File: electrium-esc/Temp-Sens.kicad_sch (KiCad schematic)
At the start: 0 parts

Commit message: Add additional connections to MCU
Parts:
- added TH? (x2): Thermistor_PTC, symbol Device:Thermistor_PTC
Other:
- company: (none) -> Electrium Mobility
- title: (none) -> BLDC Electronic Speed Controller 1.0
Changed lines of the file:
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@@
 (kicad_sch (version 20211123) (generator eeschema)
   (paper "A4")
+  (title_block
+    (title "BLDC Electronic Speed Controller 1.0")
+    (rev "ESC 1.0")
+    (company "Electrium Mobility")
+    (comment 1 "Temp Sensors")
+  )
+  (symbol (lib_id "Device:Thermistor_PTC") (at 181.61 95.25 0) (unit 1)
+    (in_bom yes) (on_board yes) (fields_autoplaced)
+    (property "Reference" "TH?" (id 0) (at 184.15 94.2974 0)
+      (effects (font (size 1.27 1.27)) (justify left))
+    )
+    (property "Value" "Thermistor_PTC" (id 1) (at 184.15 96.8374 0)
+      (effects (font (size 1.27 1.27)) (justify left))
+    )
+    (property "Footprint" "" (id 2) (at 182.88 100.33 0)
+      (effects (font (size 1.27 1.27)) (justify left) hide)
+    )
+    (property "Datasheet" "~" (id 3) (at 181.61 95.25 0)
+      (effects (font (size 1.27 1.27)) hide)
+    )
+    (pin "1")
+    (pin "2")
+  )
+  (symbol (lib_id "Device:Thermistor_PTC") (at 153.67 95.25 0) (unit 1)
+    (in_bom yes) (on_board yes) (fields_autoplaced)
+    (property "Reference" "TH?" (id 0) (at 156.21 94.2974 0)
+      (effects (font (size 1.27 1.27)) (justify left))
+    )
+    (property "Value" "Thermistor_PTC" (id 1) (at 156.21 96.8374 0)
+      (effects (font (size 1.27 1.27)) (justify left))
+    )
+    (property "Footprint" "" (id 2) (at 154.94 100.33 0)
+      (effects (font (size 1.27 1.27)) (justify left) hide)
+    )
+    (property "Datasheet" "~" (id 3) (at 153.67 95.25 0)
+      (effects (font (size 1.27 1.27)) hide)
+    )
+    (pin "1")
+    (pin "2")
+  )
 )

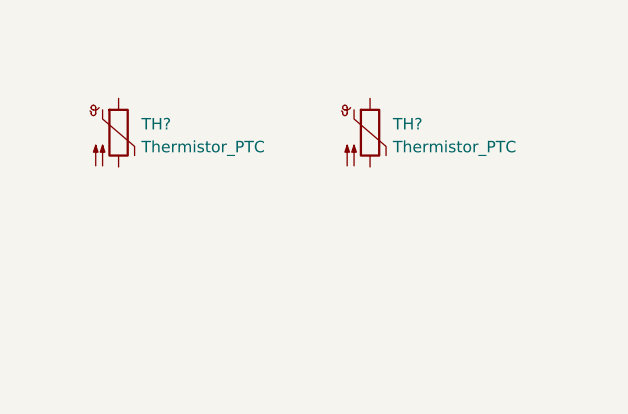
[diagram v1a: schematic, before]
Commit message: Connect Temperature Sensors
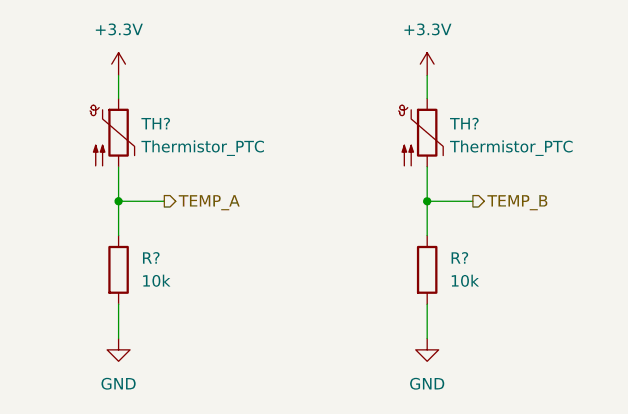
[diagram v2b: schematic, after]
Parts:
- added R? (x2): 10k, symbol Device:R
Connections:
- net +3.3V: now reaches TH?.1
- net +3.3V: now also TH?.1
- net TEMP_B: now reaches TH?.2
- net TEMP_B: now also R?.1
- net TEMP_A: now reaches TH?.2
- net TEMP_A: now also R?.1
- new net GND: R?.2, R?.2
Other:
- moved on the sheet: TH?
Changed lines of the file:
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@@
     (comment 1 "Temp Sensors")
   )
-  (symbol (lib_id "Device:Thermistor_PTC") (at 181.61 95.25 0) (unit 1)
+  (junction (at 187.96 102.87) (diameter 0) (color 0 0 0 0)
+  )
+  (junction (at 153.67 102.87) (diameter 0) (color 0 0 0 0)
+  )
+  (wire (pts (xy 153.67 102.87) (xy 158.75 102.87))
+    (stroke (width 0) (type default) (color 0 0 0 0))
+  )
+  (wire (pts (xy 153.67 88.9) (xy 153.67 91.44))
+    (stroke (width 0) (type default) (color 0 0 0 0))
+  )
+  (wire (pts (xy 153.67 114.3) (xy 153.67 118.11))
+    (stroke (width 0) (type default) (color 0 0 0 0))
+  )
+  (wire (pts (xy 153.67 102.87) (xy 153.67 106.68))
+    (stroke (width 0) (type default) (color 0 0 0 0))
+  )
+  (wire (pts (xy 187.96 102.87) (xy 187.96 106.68))
+    (stroke (width 0) (type default) (color 0 0 0 0))
+  )
+  (wire (pts (xy 187.96 114.3) (xy 187.96 118.11))
+    (stroke (width 0) (type default) (color 0 0 0 0))
+  )
+  (wire (pts (xy 187.96 88.9) (xy 187.96 91.44))
+    (stroke (width 0) (type default) (color 0 0 0 0))
+  )
+  (wire (pts (xy 187.96 99.06) (xy 187.96 102.87))
+    (stroke (width 0) (type default) (color 0 0 0 0))
+  )
+  (wire (pts (xy 187.96 102.87) (xy 193.04 102.87))
+    (stroke (width 0) (type default) (color 0 0 0 0))
+  )
+  (wire (pts (xy 153.67 99.06) (xy 153.67 102.87))
+    (stroke (width 0) (type default) (color 0 0 0 0))
+  )
+  (hierarchical_label "TEMP_B" (shape output) (at 193.04 102.87 0)
+    (effects (font (size 1.27 1.27)) (justify left))
+  )
+  (hierarchical_label "TEMP_A" (shape output) (at 158.75 102.87 0)
+    (effects (font (size 1.27 1.27)) (justify left))
+  )
+  (symbol (lib_id "power:GND") (at 153.67 118.11 0) (unit 1)
     (in_bom yes) (on_board yes) (fields_autoplaced)
-    (property "Reference" "TH?" (id 0) (at 184.15 94.2974 0)
+    (property "Reference" "#PWR?" (id 0) (at 153.67 124.46 0)
+      (effects (font (size 1.27 1.27)) hide)
+    )
+    (property "Value" "GND" (id 1) (at 153.67 123.19 0))
+    (property "Footprint" "" (id 2) (at 153.67 118.11 0)
+      (effects (font (size 1.27 1.27)) hide)
+    )
+    (property "Datasheet" "" (id 3) (at 153.67 118.11 0)
+      (effects (font (size 1.27 1.27)) hide)
+    )
+    (pin "1")
+  )
+  (symbol (lib_id "Device:Thermistor_PTC") (at 187.96 95.25 0) (unit 1)
+    (in_bom yes) (on_board yes) (fields_autoplaced)
+    (property "Reference" "TH?" (id 0) (at 190.5 94.2974 0)
       (effects (font (size 1.27 1.27)) (justify left))
     )
-    (property "Value" "Thermistor_PTC" (id 1) (at 184.15 96.8374 0)
+    (property "Value" "Thermistor_PTC" (id 1) (at 190.5 96.8374 0)
       (effects (font (size 1.27 1.27)) (justify left))
     )
-    (property "Footprint" "" (id 2) (at 182.88 100.33 0)
+    (property "Footprint" "" (id 2) (at 189.23 100.33 0)
       (effects (font (size 1.27 1.27)) (justify left) hide)
     )
-    (property "Datasheet" "~" (id 3) (at 181.61 95.25 0)
+    (property "Datasheet" "~" (id 3) (at 187.96 95.25 0)
       (effects (font (size 1.27 1.27)) hide)
     )
     (pin "1")
     (pin "2")
+  )
+  (symbol (lib_id "Device:R") (at 153.67 110.49 0) (unit 1)
+    (in_bom yes) (on_board yes) (fields_autoplaced)
+    (property "Reference" "R?" (id 0) (at 156.21 109.2199 0)
+      (effects (font (size 1.27 1.27)) (justify left))
+    )
+    (property "Value" "10k" (id 1) (at 156.21 111.7599 0)
+      (effects (font (size 1.27 1.27)) (justify left))
+    )
+    (property "Footprint" "" (id 2) (at 151.892 110.49 90)
+      (effects (font (size 1.27 1.27)) hide)
+    )
+    (property "Datasheet" "~" (id 3) (at 153.67 110.49 0)
+      (effects (font (size 1.27 1.27)) hide)
+    )
+    (pin "1")
+    (pin "2")
+  )
+  (symbol (lib_id "power:GND") (at 187.96 118.11 0) (unit 1)
+    (in_bom yes) (on_board yes) (fields_autoplaced)
+    (property "Reference" "#PWR?" (id 0) (at 187.96 124.46 0)
+      (effects (font (size 1.27 1.27)) hide)
+    )
+    (property "Value" "GND" (id 1) (at 187.96 123.19 0))
+    (property "Footprint" "" (id 2) (at 187.96 118.11 0)
+      (effects (font (size 1.27 1.27)) hide)
+    )
+    (property "Datasheet" "" (id 3) (at 187.96 118.11 0)
+      (effects (font (size 1.27 1.27)) hide)
+    )
+    (pin "1")
+  )
+  (symbol (lib_id "power:+3.3V") (at 153.67 88.9 0) (unit 1)
+    (in_bom yes) (on_board yes) (fields_autoplaced)
+    (property "Reference" "#PWR?" (id 0) (at 153.67 92.71 0)
+      (effects (font (size 1.27 1.27)) hide)
+    )
+    (property "Value" "+3.3V" (id 1) (at 153.67 83.82 0))
+    (property "Footprint" "" (id 2) (at 153.67 88.9 0)
+      (effects (font (size 1.27 1.27)) hide)
+    )
+    (property "Datasheet" "" (id 3) (at 153.67 88.9 0)
+      (effects (font (size 1.27 1.27)) hide)
+    )
+    (pin "1")
+  )
+  (symbol (lib_id "power:+3.3V") (at 187.96 88.9 0) (unit 1)
+    (in_bom yes) (on_board yes) (fields_autoplaced)
+    (property "Reference" "#PWR?" (id 0) (at 187.96 92.71 0)
+      (effects (font (size 1.27 1.27)) hide)
+    )
+    (property "Value" "+3.3V" (id 1) (at 187.96 83.82 0))
+    (property "Footprint" "" (id 2) (at 187.96 88.9 0)
+      (effects (font (size 1.27 1.27)) hide)
+    )
+    (property "Datasheet" "" (id 3) (at 187.96 88.9 0)
+      (effects (font (size 1.27 1.27)) hide)
+    )
+    (pin "1")
   )
   (symbol (lib_id "Device:Thermistor_PTC") (at 153.67 95.25 0) (unit 1)
@@
       (effects (font (size 1.27 1.27)) hide)
     )
+    (pin "1")
+    (pin "2")
+  )
+  (symbol (lib_id "Device:R") (at 187.96 110.49 0) (unit 1)
+    (in_bom yes) (on_board yes) (fields_autoplaced)
+    (property "Reference" "R?" (id 0) (at 190.5 109.2199 0)
+      (effects (font (size 1.27 1.27)) (justify left))
+    )
+    (property "Value" "10k" (id 1) (at 190.5 111.7599 0)
+      (effects (font (size 1.27 1.27)) (justify left))
+    )
+    (property "Footprint" "" (id 2) (at 186.182 110.49 90)
+      (effects (font (size 1.27 1.27)) hide)
+    )
+    (property "Datasheet" "~" (id 3) (at 187.96 110.49 0)
+      (effects (font (size 1.27 1.27)) hide)
+    )

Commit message: Modify title
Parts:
- added C? (x2): 2.2u, symbol Device:C
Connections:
- net GND: now also C?.2, C?.2
- net TEMP_A: now also C?.1
- net TEMP_B: now also C?.1
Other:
- moved on the sheet: R?
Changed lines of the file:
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@@
     (comment 1 "Temp Sensors")
   )
+  (junction (at 153.67 116.84) (diameter 0) (color 0 0 0 0)
+  )
   (junction (at 187.96 102.87) (diameter 0) (color 0 0 0 0)
   )
   (junction (at 153.67 102.87) (diameter 0) (color 0 0 0 0)
   )
+  (junction (at 187.96 116.84) (diameter 0) (color 0 0 0 0)
+  )
+  (wire (pts (xy 187.96 116.84) (xy 187.96 118.11))
+    (stroke (width 0) (type default) (color 0 0 0 0))
+  )
   (wire (pts (xy 153.67 102.87) (xy 158.75 102.87))
     (stroke (width 0) (type default) (color 0 0 0 0))
@@
     (stroke (width 0) (type default) (color 0 0 0 0))
   )
-  (wire (pts (xy 153.67 114.3) (xy 153.67 118.11))
-    (stroke (width 0) (type default) (color 0 0 0 0))
-  )
-  (wire (pts (xy 153.67 102.87) (xy 153.67 106.68))
-    (stroke (width 0) (type default) (color 0 0 0 0))
-  )
-  (wire (pts (xy 187.96 102.87) (xy 187.96 106.68))
-    (stroke (width 0) (type default) (color 0 0 0 0))
-  )
-  (wire (pts (xy 187.96 114.3) (xy 187.96 118.11))
+  (wire (pts (xy 153.67 113.03) (xy 153.67 116.84))
+    (stroke (width 0) (type default) (color 0 0 0 0))
+  )
+  (wire (pts (xy 179.07 113.03) (xy 179.07 116.84))
+    (stroke (width 0) (type default) (color 0 0 0 0))
+  )
+  (wire (pts (xy 153.67 102.87) (xy 153.67 105.41))
+    (stroke (width 0) (type default) (color 0 0 0 0))
+  )
+  (wire (pts (xy 179.07 105.41) (xy 179.07 102.87))
+    (stroke (width 0) (type default) (color 0 0 0 0))
+  )
+  (wire (pts (xy 187.96 102.87) (xy 187.96 105.41))
+    (stroke (width 0) (type default) (color 0 0 0 0))
+  )
+  (wire (pts (xy 153.67 116.84) (xy 153.67 118.11))
+    (stroke (width 0) (type default) (color 0 0 0 0))
+  )
+  (wire (pts (xy 144.78 113.03) (xy 144.78 116.84))
+    (stroke (width 0) (type default) (color 0 0 0 0))
+  )
+  (wire (pts (xy 187.96 113.03) (xy 187.96 116.84))
     (stroke (width 0) (type default) (color 0 0 0 0))
   )
@@
     (stroke (width 0) (type default) (color 0 0 0 0))
   )
+  (wire (pts (xy 144.78 105.41) (xy 144.78 102.87))
+    (stroke (width 0) (type default) (color 0 0 0 0))
+  )
+  (wire (pts (xy 179.07 102.87) (xy 187.96 102.87))
+    (stroke (width 0) (type default) (color 0 0 0 0))
+  )
+  (wire (pts (xy 144.78 116.84) (xy 153.67 116.84))
+    (stroke (width 0) (type default) (color 0 0 0 0))
+  )
   (wire (pts (xy 187.96 99.06) (xy 187.96 102.87))
     (stroke (width 0) (type default) (color 0 0 0 0))
   )
+  (wire (pts (xy 179.07 116.84) (xy 187.96 116.84))
+    (stroke (width 0) (type default) (color 0 0 0 0))
+  )
   (wire (pts (xy 187.96 102.87) (xy 193.04 102.87))
     (stroke (width 0) (type default) (color 0 0 0 0))
@@
   (wire (pts (xy 153.67 99.06) (xy 153.67 102.87))
     (stroke (width 0) (type default) (color 0 0 0 0))
+  )
+  (wire (pts (xy 144.78 102.87) (xy 153.67 102.87))
+    (stroke (width 0) (type default) (color 0 0 0 0))
+  )
+  (label "Temperature Resistors 10k" (at 158.75 90.17 0)
+    (effects (font (size 1.27 1.27)) (justify left bottom))
   )
   (hierarchical_label "TEMP_B" (shape output) (at 193.04 102.87 0)
@@
     (pin "2")
   )
-  (symbol (lib_id "Device:R") (at 153.67 110.49 0) (unit 1)
-    (in_bom yes) (on_board yes) (fields_autoplaced)
-    (property "Reference" "R?" (id 0) (at 156.21 109.2199 0)
-      (effects (font (size 1.27 1.27)) (justify left))
-    )
-    (property "Value" "10k" (id 1) (at 156.21 111.7599 0)
-      (effects (font (size 1.27 1.27)) (justify left))
-    )
-    (property "Footprint" "" (id 2) (at 151.892 110.49 90)
-      (effects (font (size 1.27 1.27)) hide)
-    )
-    (property "Datasheet" "~" (id 3) (at 153.67 110.49 0)
+  (symbol (lib_id "Device:R") (at 153.67 109.22 0) (unit 1)
+    (in_bom yes) (on_board yes) (fields_autoplaced)
+    (property "Reference" "R?" (id 0) (at 156.21 107.9499 0)
+      (effects (font (size 1.27 1.27)) (justify left))
+    )
+    (property "Value" "10k" (id 1) (at 156.21 110.4899 0)
+      (effects (font (size 1.27 1.27)) (justify left))
+    )
+    (property "Footprint" "" (id 2) (at 151.892 109.22 90)
+      (effects (font (size 1.27 1.27)) hide)
+    )
+    (property "Datasheet" "~" (id 3) (at 153.67 109.22 0)
+      (effects (font (size 1.27 1.27)) hide)
+    )
+    (pin "1")
+    (pin "2")
+  )
+  (symbol (lib_id "Device:C") (at 179.07 109.22 0) (unit 1)
+    (in_bom yes) (on_board yes)
+    (property "Reference" "C?" (id 0) (at 181.61 107.95 0)
+      (effects (font (size 1.27 1.27)) (justify left))
+    )
+    (property "Value" "2.2u" (id 1) (at 181.61 110.49 0)
+      (effects (font (size 1.27 1.27)) (justify left))
+    )
+    (property "Footprint" "" (id 2) (at 180.0352 113.03 0)
+      (effects (font (size 1.27 1.27)) hide)
+    )
+    (property "Datasheet" "~" (id 3) (at 179.07 109.22 0)
       (effects (font (size 1.27 1.27)) hide)
     )
@@
     (pin "1")
   )
+  (symbol (lib_id "Device:C") (at 144.78 109.22 0) (unit 1)
+    (in_bom yes) (on_board yes)
+    (property "Reference" "C?" (id 0) (at 147.32 107.95 0)
+      (effects (font (size 1.27 1.27)) (justify left))
+    )
+    (property "Value" "2.2u" (id 1) (at 147.32 110.49 0)
+      (effects (font (size 1.27 1.27)) (justify left))
+    )
+    (property "Footprint" "" (id 2) (at 145.7452 113.03 0)
+      (effects (font (size 1.27 1.27)) hide)
+    )
+    (property "Datasheet" "~" (id 3) (at 144.78 109.22 0)
+      (effects (font (size 1.27 1.27)) hide)
+    )
+    (pin "1")
+    (pin "2")
+  )
   (symbol (lib_id "Device:Thermistor_PTC") (at 153.67 95.25 0) (unit 1)
     (in_bom yes) (on_board yes) (fields_autoplaced)
@@
     (pin "2")
   )
-  (symbol (lib_id "Device:R") (at 187.96 110.49 0) (unit 1)
-    (in_bom yes) (on_board yes) (fields_autoplaced)
-    (property "Reference" "R?" (id 0) (at 190.5 109.2199 0)
-      (effects (font (size 1.27 1.27)) (justify left))
-    )
-    (property "Value" "10k" (id 1) (at 190.5 111.7599 0)
-      (effects (font (size 1.27 1.27)) (justify left))
-    )
-    (property "Footprint" "" (id 2) (at 186.182 110.49 90)
-      (effects (font (size 1.27 1.27)) hide)
-    )
-    (property "Datasheet" "~" (id 3) (at 187.96 110.49 0)
-      (effects (font (size 1.27 1.27)) hide)
-    )
+  (symbol (lib_id "Device:R") (at 187.96 109.22 0) (unit 1)
+    (in_bom yes) (on_board yes) (fields_autoplaced)
+    (property "Reference" "R?" (id 0) (at 190.5 107.9499 0)
+      (effects (font (size 1.27 1.27)) (justify left))
+    )
+    (property "Value" "10k" (id 1) (at 190.5 110.4899 0)
+      (effects (font (size 1.27 1.27)) (justify left))
+    )
+    (property "Footprint" "" (id 2) (at 186.182 109.22 90)
+      (effects (font (size 1.27 1.27)) hide)
+    )
+    (property "Datasheet" "~" (id 3) (at 187.96 109.22 0)
+      (effects (font (size 1.27 1.27)) hide)
+    )

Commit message: Fix Error
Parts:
- C75, C76: renamed from C?; footprint (none) -> Capacitor_SMD:C_0603_1608Metric
- R60, R61: renamed from R?; footprint (none) -> Resistor_SMD:R_0603_1608Metric
- TH1, TH2: renamed from TH?; footprint (none) -> Resistor_SMD:R_0603_1608Metric
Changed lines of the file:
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@@
     (stroke (width 0) (type default) (color 0 0 0 0))
-  )
-  (label "Temperature Resistors 10k" (at 158.75 90.17 0)
-    (effects (font (size 1.27 1.27)) (justify left bottom))
   )
   (hierarchical_label "TEMP_B" (shape output) (at 193.04 102.87 0)
@@
   (symbol (lib_id "power:GND") (at 153.67 118.11 0) (unit 1)
     (in_bom yes) (on_board yes) (fields_autoplaced)
-    (property "Reference" "#PWR?" (id 0) (at 153.67 124.46 0)
+    (property "Reference" "#PWR0169" (id 0) (at 153.67 124.46 0)
       (effects (font (size 1.27 1.27)) hide)
     )
@@
   (symbol (lib_id "Device:Thermistor_PTC") (at 187.96 95.25 0) (unit 1)
     (in_bom yes) (on_board yes) (fields_autoplaced)
-    (property "Reference" "TH?" (id 0) (at 190.5 94.2974 0)
+    (property "Reference" "TH2" (id 0) (at 190.5 94.2974 0)
       (effects (font (size 1.27 1.27)) (justify left))
     )
@@
       (effects (font (size 1.27 1.27)) (justify left))
     )
-    (property "Footprint" "" (id 2) (at 189.23 100.33 0)
+    (property "Footprint" "Resistor_SMD:R_0603_1608Metric" (id 2) (at 189.23 100.33 0)
       (effects (font (size 1.27 1.27)) (justify left) hide)
     )
@@
   (symbol (lib_id "Device:R") (at 153.67 109.22 0) (unit 1)
     (in_bom yes) (on_board yes) (fields_autoplaced)
-    (property "Reference" "R?" (id 0) (at 156.21 107.9499 0)
+    (property "Reference" "R60" (id 0) (at 156.21 107.9499 0)
       (effects (font (size 1.27 1.27)) (justify left))
     )
@@
       (effects (font (size 1.27 1.27)) (justify left))
     )
-    (property "Footprint" "" (id 2) (at 151.892 109.22 90)
+    (property "Footprint" "Resistor_SMD:R_0603_1608Metric" (id 2) (at 151.892 109.22 90)
       (effects (font (size 1.27 1.27)) hide)
     )
@@
   (symbol (lib_id "Device:C") (at 179.07 109.22 0) (unit 1)
     (in_bom yes) (on_board yes)
-    (property "Reference" "C?" (id 0) (at 181.61 107.95 0)
+    (property "Reference" "C76" (id 0) (at 181.61 107.95 0)
       (effects (font (size 1.27 1.27)) (justify left))
     )
@@
       (effects (font (size 1.27 1.27)) (justify left))
     )
-    (property "Footprint" "" (id 2) (at 180.0352 113.03 0)
+    (property "Footprint" "Capacitor_SMD:C_0603_1608Metric" (id 2) (at 180.0352 113.03 0)
       (effects (font (size 1.27 1.27)) hide)
     )
@@
   (symbol (lib_id "power:GND") (at 187.96 118.11 0) (unit 1)
     (in_bom yes) (on_board yes) (fields_autoplaced)
-    (property "Reference" "#PWR?" (id 0) (at 187.96 124.46 0)
+    (property "Reference" "#PWR0167" (id 0) (at 187.96 124.46 0)
       (effects (font (size 1.27 1.27)) hide)
     )
@@
   (symbol (lib_id "power:+3.3V") (at 153.67 88.9 0) (unit 1)
     (in_bom yes) (on_board yes) (fields_autoplaced)
-    (property "Reference" "#PWR?" (id 0) (at 153.67 92.71 0)
+    (property "Reference" "#PWR0168" (id 0) (at 153.67 92.71 0)
       (effects (font (size 1.27 1.27)) hide)
     )
@@
   (symbol (lib_id "power:+3.3V") (at 187.96 88.9 0) (unit 1)
     (in_bom yes) (on_board yes) (fields_autoplaced)
-    (property "Reference" "#PWR?" (id 0) (at 187.96 92.71 0)
+    (property "Reference" "#PWR0170" (id 0) (at 187.96 92.71 0)
       (effects (font (size 1.27 1.27)) hide)
     )
@@
   (symbol (lib_id "Device:C") (at 144.78 109.22 0) (unit 1)
     (in_bom yes) (on_board yes)
-    (property "Reference" "C?" (id 0) (at 147.32 107.95 0)
+    (property "Reference" "C75" (id 0) (at 147.32 107.95 0)
       (effects (font (size 1.27 1.27)) (justify left))
     )
@@
       (effects (font (size 1.27 1.27)) (justify left))
     )
-    (property "Footprint" "" (id 2) (at 145.7452 113.03 0)
+    (property "Footprint" "Capacitor_SMD:C_0603_1608Metric" (id 2) (at 145.7452 113.03 0)
       (effects (font (size 1.27 1.27)) hide)
     )
@@
   (symbol (lib_id "Device:Thermistor_PTC") (at 153.67 95.25 0) (unit 1)
     (in_bom yes) (on_board yes) (fields_autoplaced)
-    (property "Reference" "TH?" (id 0) (at 156.21 94.2974 0)
+    (property "Reference" "TH1" (id 0) (at 156.21 94.2974 0)
       (effects (font (size 1.27 1.27)) (justify left))
     )
@@
       (effects (font (size 1.27 1.27)) (justify left))
     )
-    (property "Footprint" "" (id 2) (at 154.94 100.33 0)
+    (property "Footprint" "Resistor_SMD:R_0603_1608Metric" (id 2) (at 154.94 100.33 0)
       (effects (font (size 1.27 1.27)) (justify left) hide)
     )
@@
   (symbol (lib_id "Device:R") (at 187.96 109.22 0) (unit 1)
     (in_bom yes) (on_board yes) (fields_autoplaced)
-    (property "Reference" "R?" (id 0) (at 190.5 107.9499 0)
+    (property "Reference" "R61" (id 0) (at 190.5 107.9499 0)
       (effects (font (size 1.27 1.27)) (justify left))
     )
@@
       (effects (font (size 1.27 1.27)) (justify left))
     )
-    (property "Footprint" "" (id 2) (at 186.182 109.22 90)
+    (property "Footprint" "Resistor_SMD:R_0603_1608Metric" (id 2) (at 186.182 109.22 90)
       (effects (font (size 1.27 1.27)) hide)
     )
